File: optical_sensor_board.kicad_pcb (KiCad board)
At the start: 2 copper layers, 67.5 x 45.5 mm, 18 parts, among them J2 Conn_01x09_Socket, U1 PMW3389DM‐T3QU, U3 LM317L_SOT-89

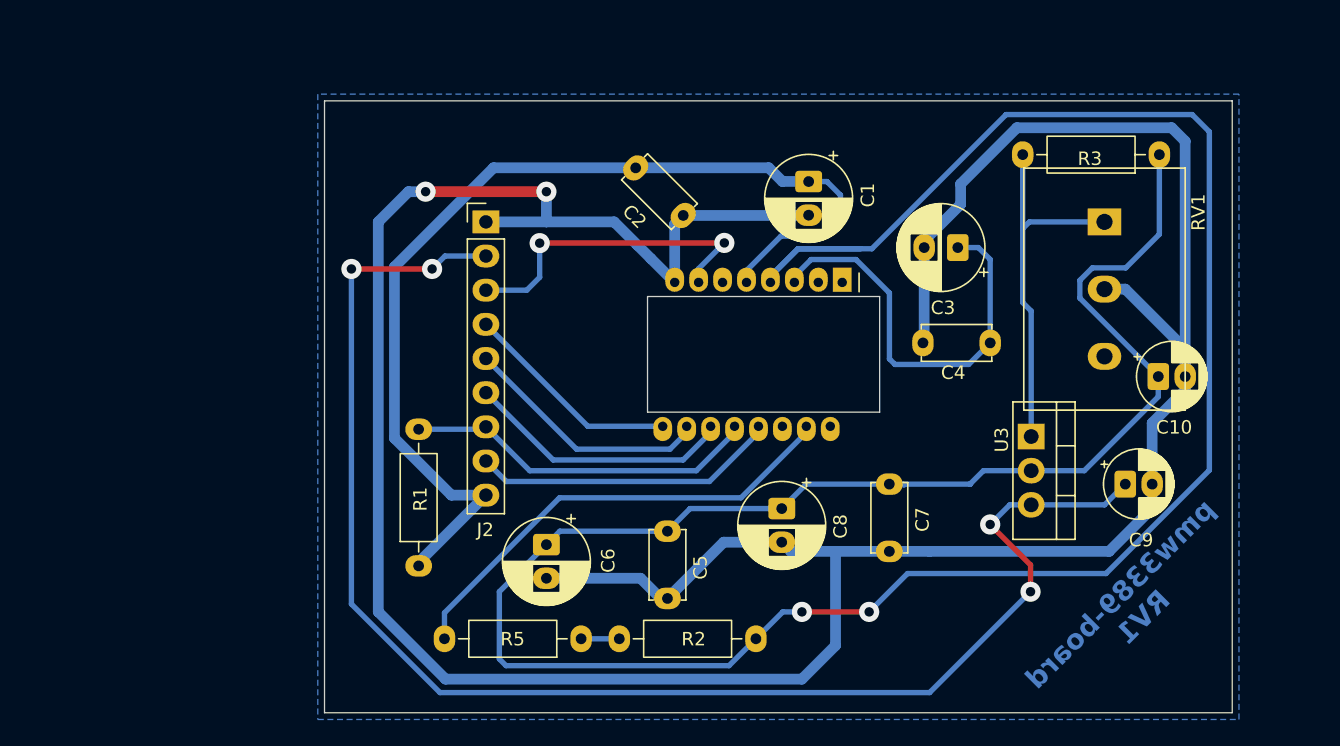
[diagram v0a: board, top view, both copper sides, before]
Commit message: TestPoint in Schematic
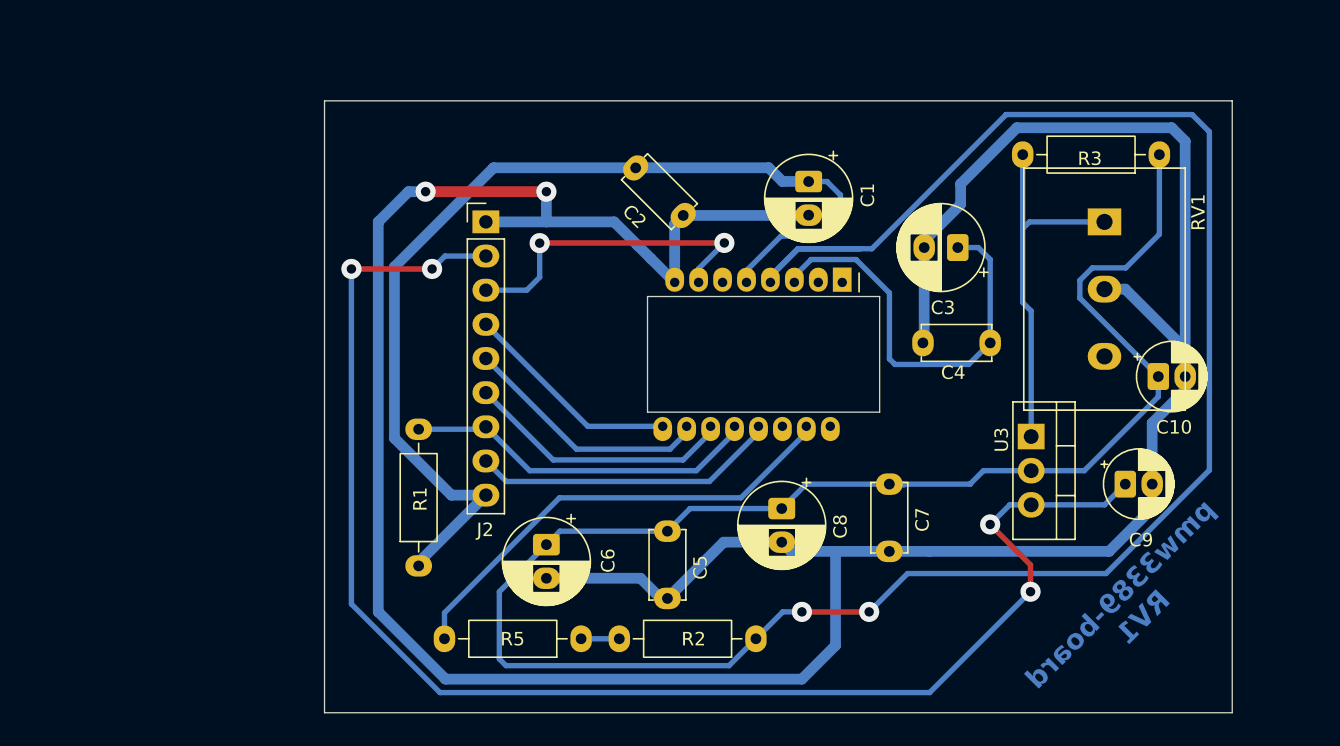
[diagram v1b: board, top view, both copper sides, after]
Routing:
- removed copper zone on B.Cu, net GND
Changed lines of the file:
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@@
 		(net 15)
-	)
-	(zone
-		(net 2)
-		(net_name "GND")
-		(layer "B.Cu")
-		(hatch edge 0.5)
-		(connect_pads
-			(clearance 0.5)
-		)
-		(min_thickness 0.25)
-		(filled_areas_thickness no)
-		(fill yes
-			(thermal_gap 0.5)
-			(thermal_bridge_width 0.5)
-		)
-		(polygon
-			(pts
-				(xy 111.5 56.5) (xy 111.5 103) (xy 180 103) (xy 180 56.5)
-			)
-		)
 	)
 	(embedded_fonts no)

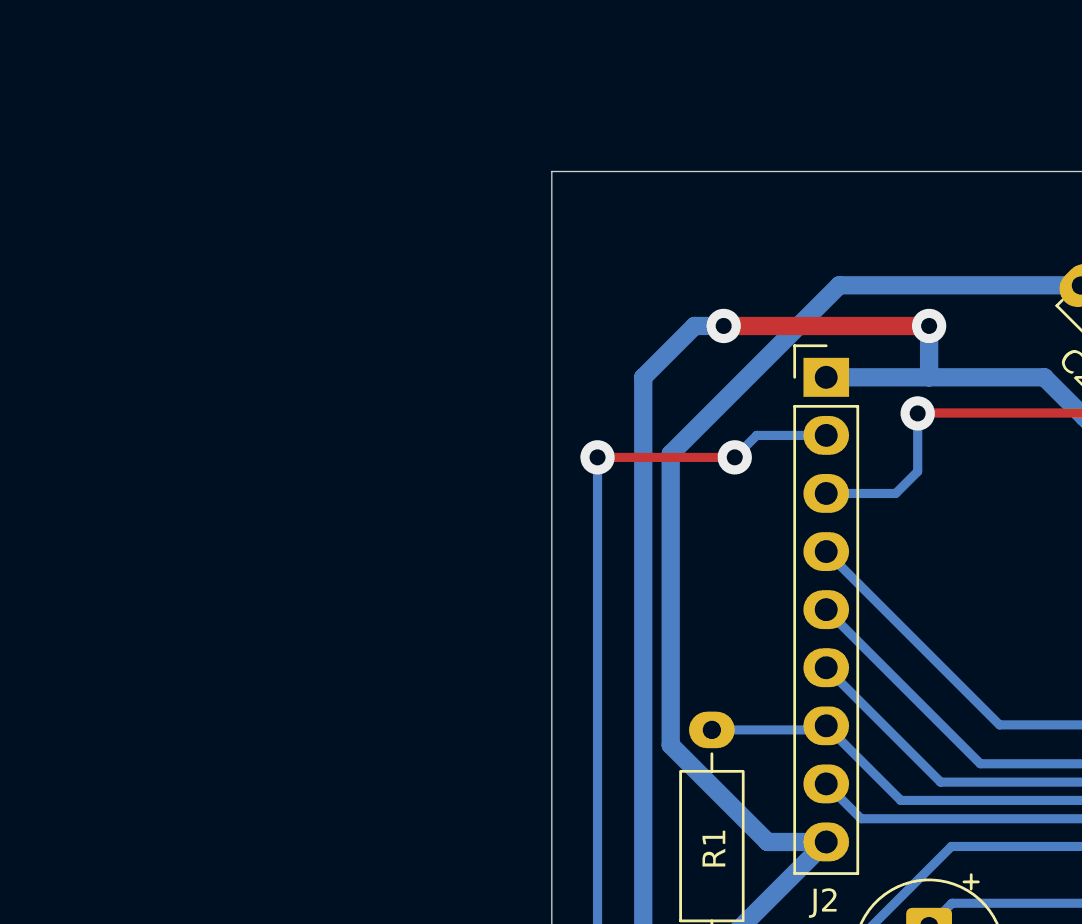
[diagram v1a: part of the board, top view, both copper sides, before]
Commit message: start TestPoint routing
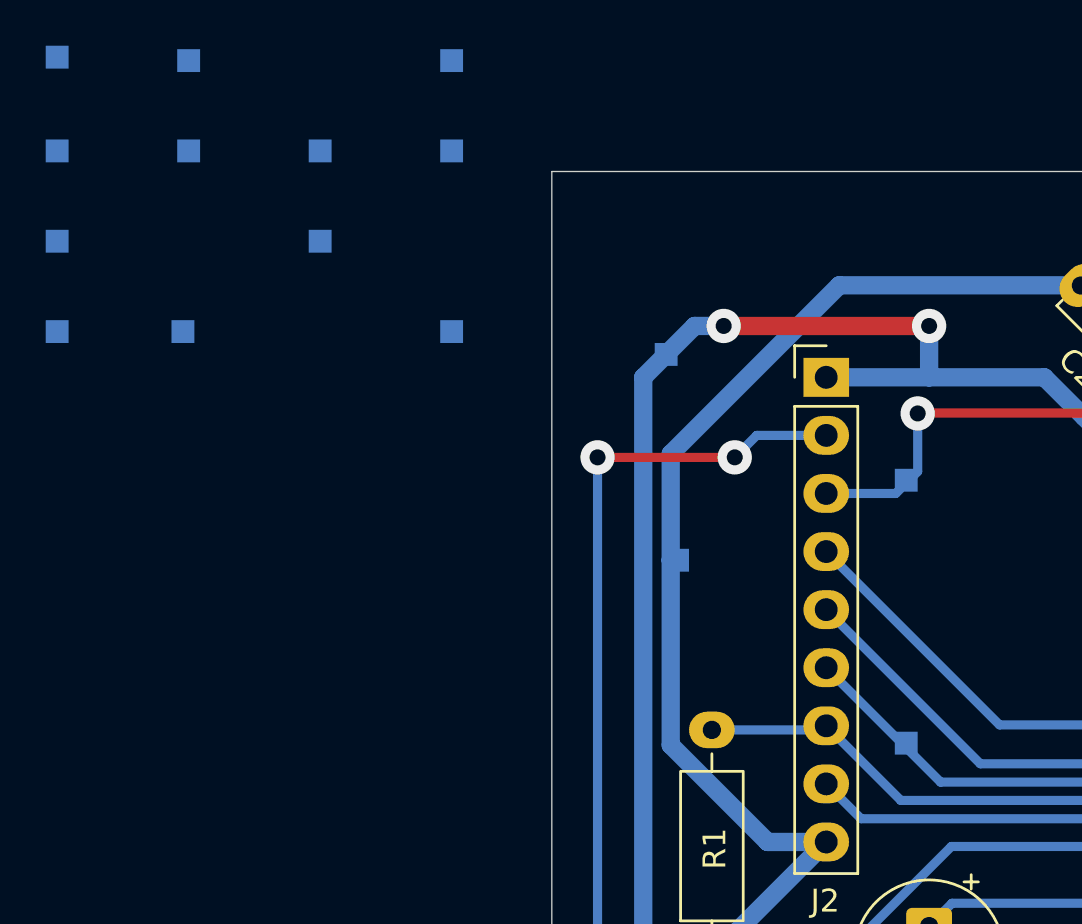
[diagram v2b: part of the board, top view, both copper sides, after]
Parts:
- added TP1: T_1V9, TestPoint:TestPoint_Pad_1.0x1.0mm, B.Cu at (107.6, 52.1)
- added TP10: T_NCS, TestPoint:TestPoint_Pad_1.0x1.0mm, B.Cu at (96.1, 56.1)
- added TP11: T_3V3, TestPoint:TestPoint_Pad_1.0x1.0mm, B.Cu at (117.5, 74.0)
- added TP12: T_GND, TestPoint:TestPoint_Pad_1.0x1.0mm, B.Cu at (95.9, 64.0)
- added TP13: T_VDDPIX, TestPoint:TestPoint_Pad_1.0x1.0mm, B.Cu at (90.4, 52.0)
- added TP14: T_VDDIO, TestPoint:TestPoint_Pad_1.0x1.0mm, B.Cu at (90.4, 56.1)
- added TP15: T_1V9, TestPoint:TestPoint_Pad_1.0x1.0mm, B.Cu at (90.4, 60.0)
- added TP16: T_VDD, TestPoint:TestPoint_Pad_1.0x1.0mm, B.Cu at (90.4, 64.0)
- added TP2: T_1V9, TestPoint:TestPoint_Pad_1.0x1.0mm, B.Cu at (107.6, 56.1)
- added TP3: T_GND, TestPoint:TestPoint_Pad_1.0x1.0mm, B.Cu at (117.0, 65.0)
- added TP4: T_5V, TestPoint:TestPoint_Pad_1.0x1.0mm, B.Cu at (107.6, 64.0)
- added TP5: T_NRESET, TestPoint:TestPoint_Pad_1.0x1.0mm, B.Cu at (127.5, 70.5)
- added TP6: T_MOTION, TestPoint:TestPoint_Pad_1.0x1.0mm, B.Cu at (101.9, 56.1)
- added TP7: T_SCLK, TestPoint:TestPoint_Pad_1.0x1.0mm, B.Cu at (101.9, 60.0)
- added TP8: T_MOSI, TestPoint:TestPoint_Pad_1.0x1.0mm, B.Cu at (127.5, 82.0)
- added TP9: T_MISO, TestPoint:TestPoint_Pad_1.0x1.0mm, B.Cu at (96.1, 52.1)

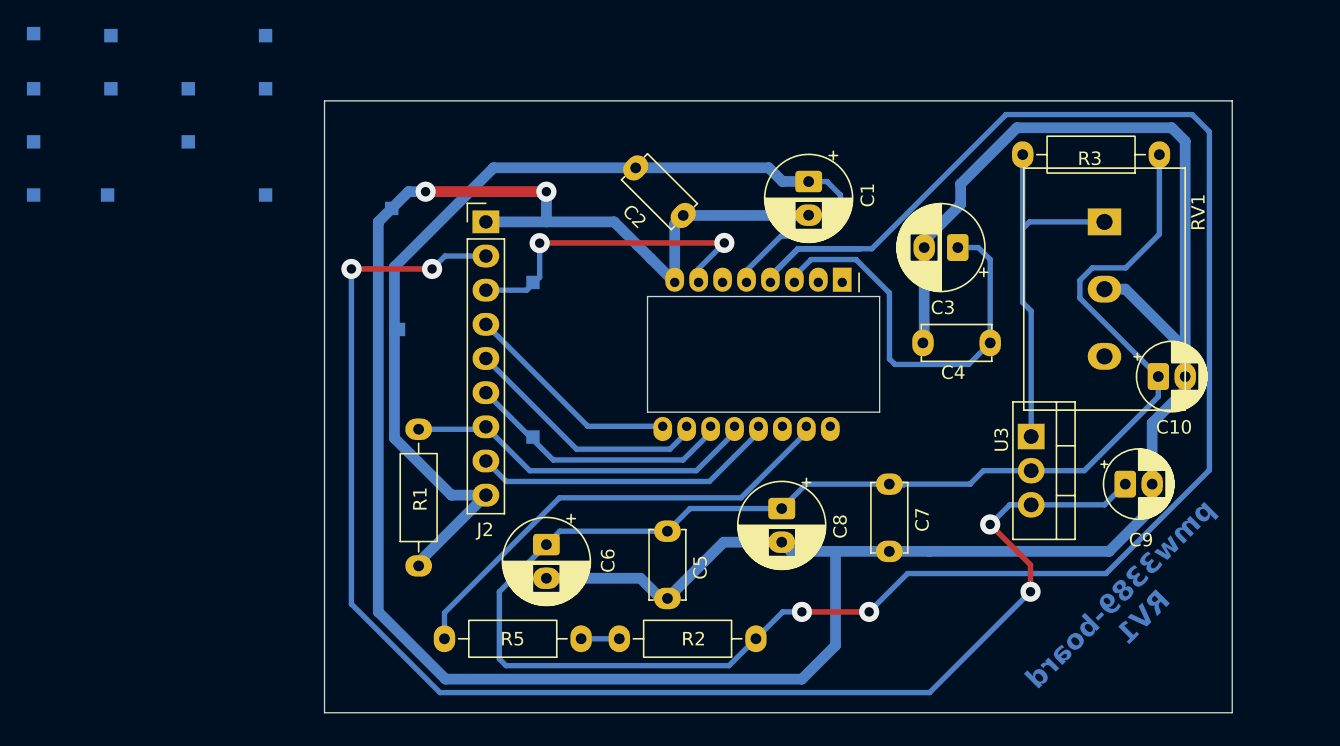
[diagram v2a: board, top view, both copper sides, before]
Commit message: TestPoint routed
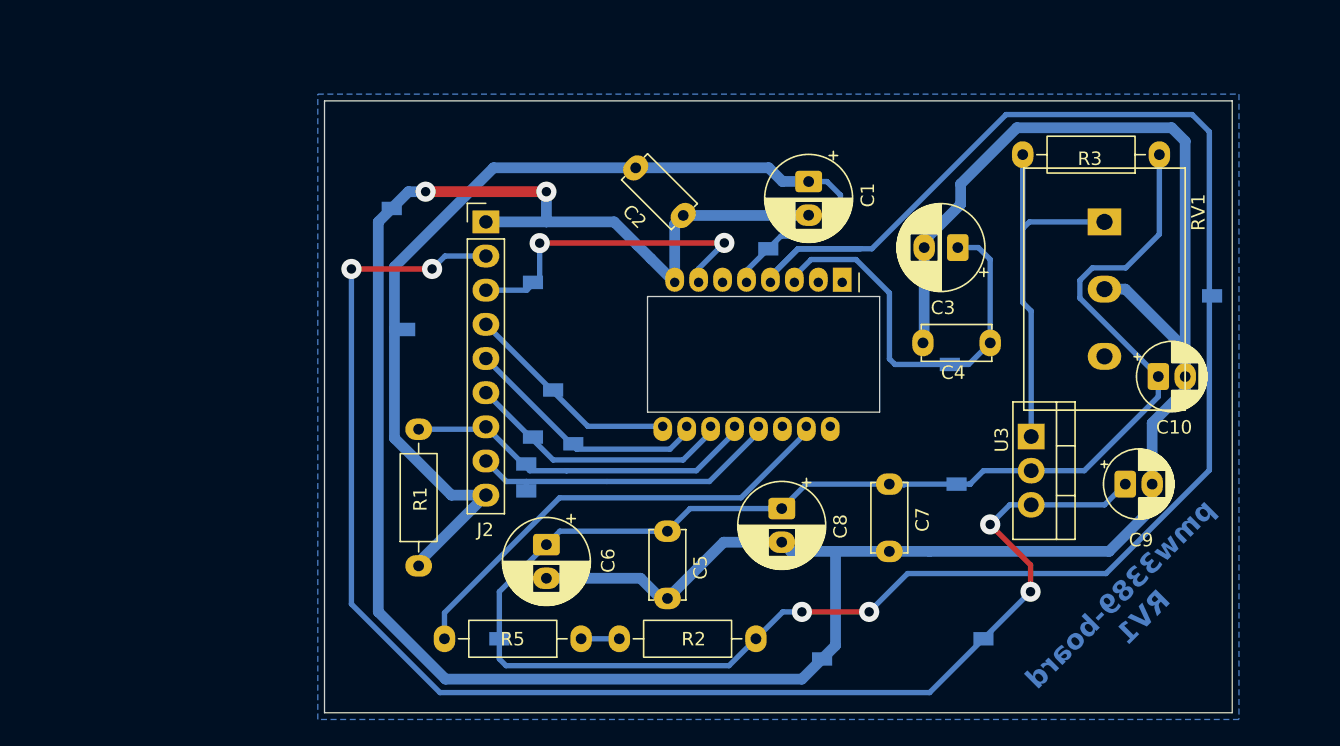
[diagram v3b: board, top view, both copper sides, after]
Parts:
- removed TP1: T_1V9, TestPoint:TestPoint_Pad_1.0x1.0mm
- moved TP16 88.0 mm to (178.0, 71.5), turned to 0 degrees
- moved TP13 72.4 mm to (158.5, 76.6)
- moved TP12 63.3 mm to (149.0, 98.5)
- moved TP4 62.8 mm to (161.0, 97.0)
- moved TP2 59.2 mm to (159.0, 85.5)
- moved TP14 55.9 mm to (145.0, 68.0)
- moved TP15 50.6 mm to (125.0, 97.0)
- moved TP9 44.4 mm to (127.0, 84.0)
- moved TP10 43.0 mm to (127.0, 86.0)
- moved TP7 36.4 mm to (130.5, 82.5)
- moved TP6 35.2 mm to (129.0, 78.5)
- moved TP11 0.50 mm to (118.0, 74.0)
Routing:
- net NCS: track 22.9 -> 23.6 mm
- net VDDPIX: track 31.3 -> 31.8 mm
- net VDDIO: track 77.9 -> 78.4 mm
- added copper zone on B.Cu, net GND
